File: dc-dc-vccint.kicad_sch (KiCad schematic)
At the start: 61 parts, among them U36 MP8796B, U4 MP8796B

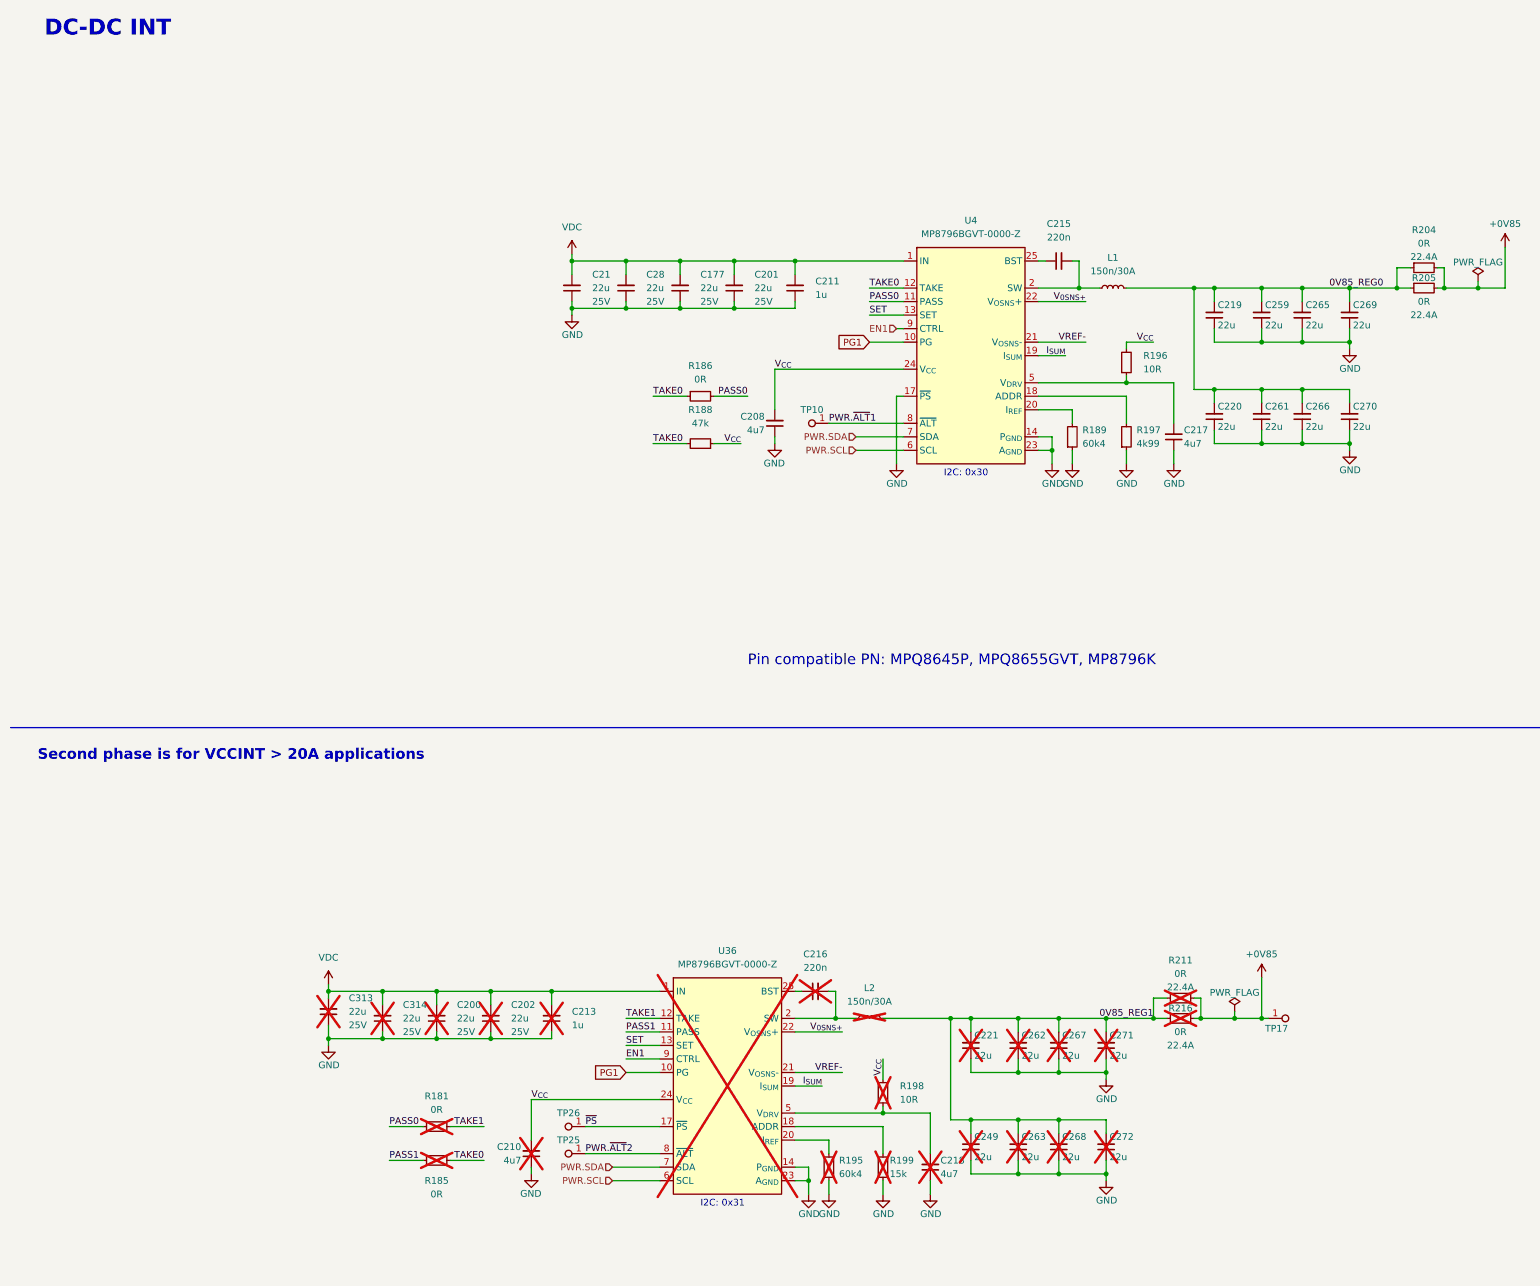
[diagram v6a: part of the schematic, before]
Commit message: [#68016] Mark U36 and its circuit as populated
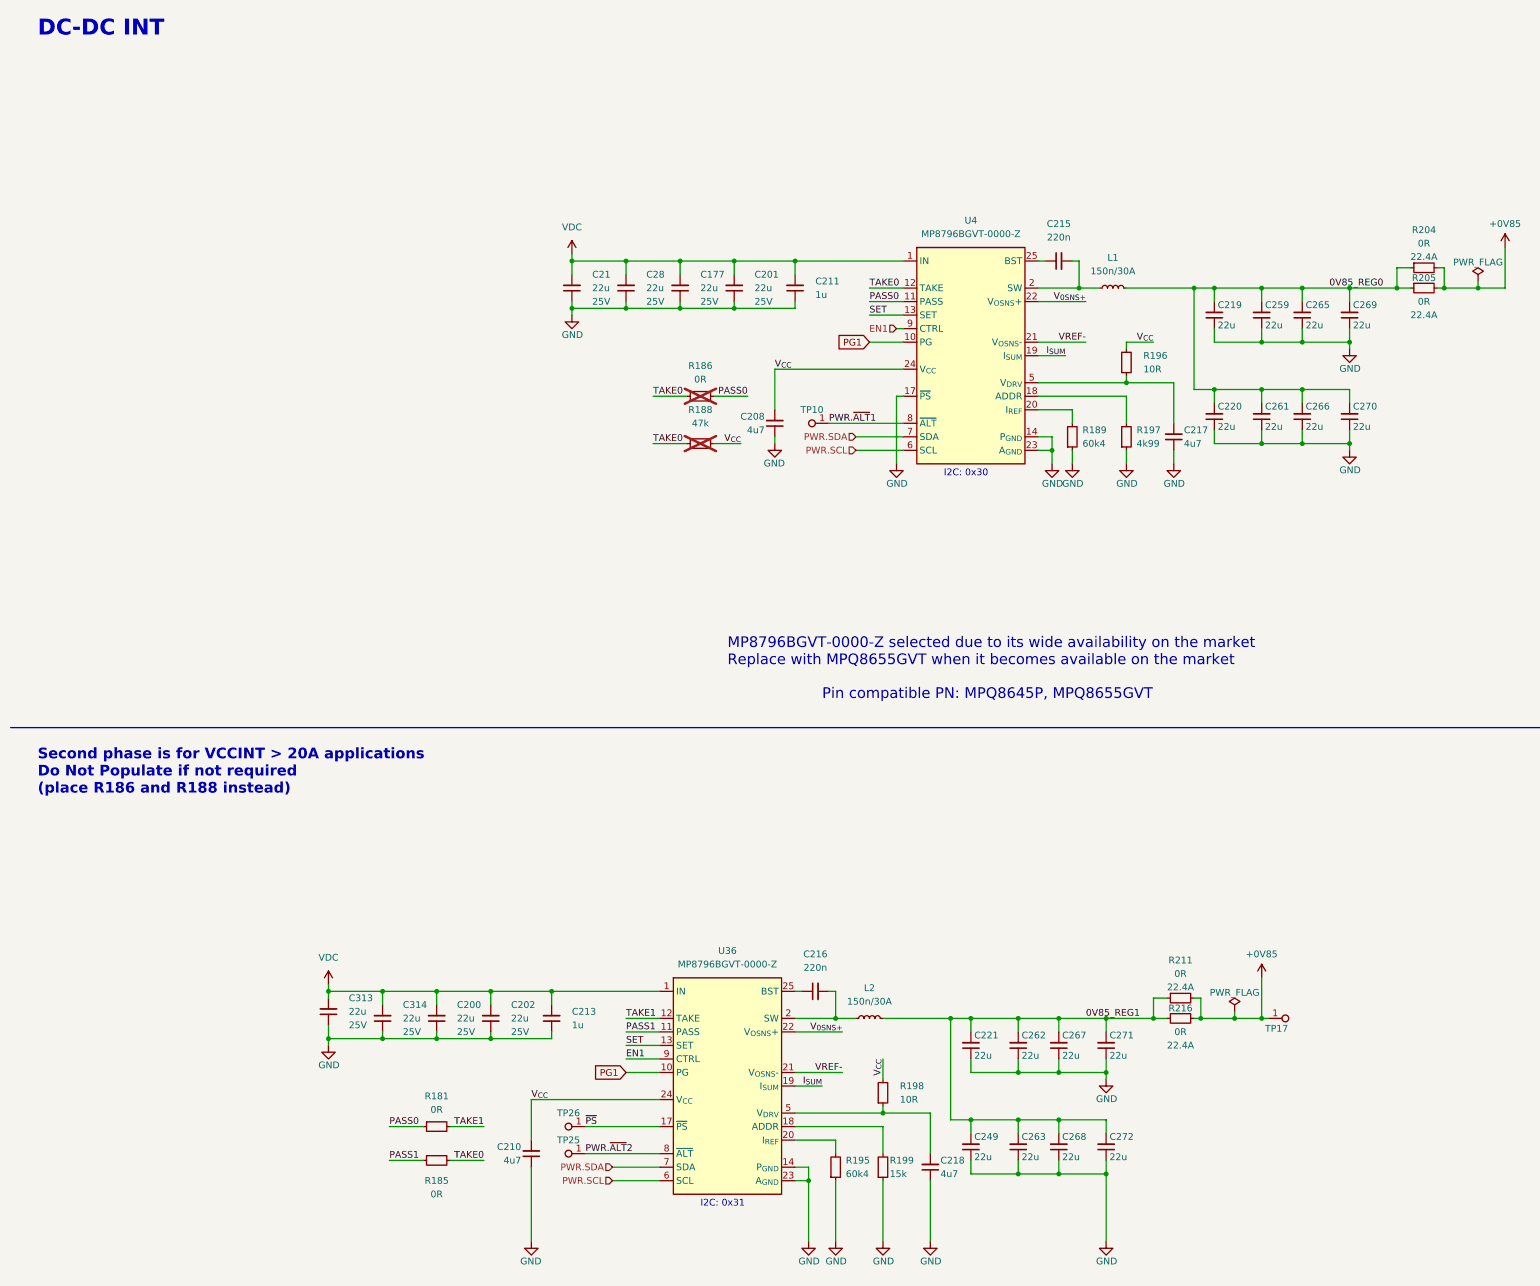
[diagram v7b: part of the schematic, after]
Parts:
- C200, C202, C210, C213, C216, C218, C221, C249, C262, C263, C267, C268, C271, C272, C313, C314, L2, R181, R185, R195, R198, R199, R211, R216, U36: now fitted
- R186, R188: now not fitted
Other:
- note added: "MP8796BGVT-0000-Z selected due to its wide availability on the market Replace with MPQ8655GVT when it becomes available on the market"
- note added: "Pin compatible PN: MPQ8645P, MPQ8655GVT"
- note added: "Second phase is for VCCINT > 20A applications Do Not Populate if not required (place R186 and R188 instead)"
- note removed: "Pin compatible PN: MPQ8645P, MPQ8655GVT, MP8796K"
- note removed: "Second phase is for VCCINT > 20A applications"
